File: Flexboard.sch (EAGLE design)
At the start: 324 parts, among them U1 MK20DN512VLQ10

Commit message: Routed LED ROW nets
PCB has not had led traces routed, but LED row nets are routed in
schematic
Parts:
- added SJ_LED_R1_0, SJ_LED_R2_0, SJ_LED_R2_1, SJ_LED_R3_1, SJ_LED_R4_0, SJ_LED_R4_1, SJ_LED_R5_0, SJ_LED_R5_1, SJ_LED_R6_0, SJ_LED_R6_1, SJ__LED_R3_0: (no value), jumper:SJW
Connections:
- new net LED_ROW_0: KEY_1.LED+, KEY_10.LED+, KEY_11.LED+, KEY_12.LED+, KEY_13.LED+, KEY_14.LED+, KEY_15.LED+, KEY_16.LED+, KEY_17.LED+, KEY_18.LED+, KEY_19.LED+, KEY_2.LED+, KEY_20.LED+, KEY_3.LED+, KEY_4.LED+, KEY_5.LED+, KEY_6.LED+, KEY_7.LED+, KEY_8.LED+, KEY_9.LED+
- new net LED_ROW_1: KEY_21.LED+, KEY_22.LED+, SJ_LED_R1_0.2
- new net LED_ROW_2: KEY_41.LED+, KEY_42.LED+, SJ_LED_R2_0.2
- new net LED_ROW_3: KEY_64.LED+, KEY_65.LED+, SJ__LED_R3_0.2
- new net LED_ROW_4: KEY_87.LED+, KEY_88.LED+, SJ_LED_R4_0.2
- new net LED_ROW_5: KEY_109.LED+, KEY_110.LED+, SJ_LED_R5_0.2
- new net LED_ROW_6: KEY_129.LED+, KEY_130.LED+, SJ_LED_R6_0.2
- new net N$1: KEY_66.LED+, KEY_67.LED+, KEY_68.LED+, KEY_69.LED+, KEY_70.LED+, KEY_71.LED+, KEY_72.LED+, KEY_73.LED+, KEY_74.LED+, KEY_75.LED+, KEY_76.LED+, KEY_77.LED+, KEY_78.LED+, KEY_79.LED+, KEY_80.LED+, KEY_81.LED+, KEY_82.LED+, SJ_LED_R3_1.2, SJ__LED_R3_0.1
- new net N$170: KEY_60.LED+, KEY_61.LED+, KEY_62.LED+, KEY_63.LED+, SJ_LED_R2_1.1
- new net N$173: KEY_83.LED+, KEY_84.LED+, KEY_85.LED+, KEY_86.LED+, SJ_LED_R3_1.1
- new net N$177: KEY_100.LED+, KEY_101.LED+, KEY_102.LED+, KEY_103.LED+, KEY_104.LED+, KEY_89.LED+, KEY_90.LED+, KEY_91.LED+, KEY_92.LED+, KEY_93.LED+, KEY_94.LED+, KEY_95.LED+, KEY_96.LED+, KEY_97.LED+, KEY_98.LED+, KEY_99.LED+, SJ_LED_R4_0.1, SJ_LED_R4_1.2
- new net N$179: KEY_105.LED+, KEY_106.LED+, KEY_107.LED+, KEY_108.LED+, SJ_LED_R4_1.1
- new net N$181: KEY_111.LED+, KEY_112.LED+, KEY_113.LED+, KEY_114.LED+, KEY_115.LED+, KEY_116.LED+, KEY_117.LED+, KEY_118.LED+, KEY_119.LED+, KEY_120.LED+, KEY_121.LED+, KEY_122.LED+, KEY_123.LED+, KEY_124.LED+, KEY_125.LED+, SJ_LED_R5_0.1, SJ_LED_R5_1.2
- new net N$182: KEY_126.LED+, KEY_127.LED+, KEY_128.LED+, SJ_LED_R5_1.1
- new net N$184: KEY_131.LED+, KEY_132.LED+, KEY_133.LED+, KEY_134.LED+, KEY_135.LED+, KEY_136.LED+, KEY_137.LED+, KEY_138.LED+, KEY_139.LED+, KEY_140.LED+, KEY_141.LED+, SJ_LED_R6_0.1, SJ_LED_R6_1.2
- new net N$185: KEY_142.LED+, KEY_143.LED+, KEY_144.LED+, KEY_145.LED+, SJ_LED_R6_1.1
- new net N$2: KEY_23.LED+, KEY_24.LED+, KEY_25.LED+, KEY_26.LED+, KEY_27.LED+, KEY_28.LED+, KEY_29.LED+, KEY_30.LED+, KEY_31.LED+, KEY_32.LED+, KEY_33.LED+, KEY_34.LED+, KEY_35.LED+, KEY_36.LED+, KEY_37.LED+, KEY_38.LED+, KEY_39.LED+, KEY_40.LED+, SJ_LED_R1_0.1
- new net N$61: KEY_43.LED+, KEY_44.LED+, KEY_45.LED+, KEY_46.LED+, KEY_47.LED+, KEY_48.LED+, KEY_49.LED+, KEY_50.LED+, KEY_51.LED+, KEY_52.LED+, KEY_53.LED+, KEY_54.LED+, KEY_55.LED+, KEY_56.LED+, KEY_57.LED+, KEY_58.LED+, KEY_59.LED+, SJ_LED_R2_0.1, SJ_LED_R2_1.2
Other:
- moved on the sheet: D129, D130, D131, D132, D133, D134, D135, D136, D137, D138, D139, D140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

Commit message: Routed Column Nets for LEDs
No LED traces routed on board, but all nets are routed for columns and
rows in schematic
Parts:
- added SJ_LED_C1, SJ_LED_C10, SJ_LED_C11, SJ_LED_C12, SJ_LED_C13, SJ_LED_C14, SJ_LED_C15, SJ_LED_C16, SJ_LED_C17, SJ_LED_C18, SJ_LED_C2, SJ_LED_C3, SJ_LED_C4, SJ_LED_C5, SJ_LED_C6, SJ_LED_C7, SJ_LED_C8, SJ_LED_C9: (no value), jumper:SJW
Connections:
- new net LED_COL_0: KEY_1.LED-, KEY_109.LED-, KEY_129.LED-, KEY_21.LED-, KEY_41.LED-, KEY_64.LED-, KEY_87.LED-
- new net LED_COL_1: KEY_110.LED-, KEY_130.LED-, KEY_2.LED-, KEY_22.LED-, KEY_42.LED-, KEY_65.LED-, KEY_88.LED-
- new net LED_COL_10: KEY_119.LED-, KEY_31.LED-, KEY_31_OFFSET.LED-, KEY_51.LED-, KEY_74.LED-, KEY_97.LED-, SJ_LED_C10.1
- new net LED_COL_11: KEY_120.LED-, KEY_135.LED-, KEY_32.LED-, KEY_32_OFFSET.LED-, KEY_52.LED-, KEY_75.LED-, KEY_98.LED-, SJ_LED_C11.1
- new net LED_COL_12: KEY_121.LED-, KEY_136.LED-, KEY_33.LED-, KEY_33_OFFSET.LED-, KEY_53.LED-, KEY_76.LED-, KEY_99.LED-, SJ_LED_C12.1
- new net LED_COL_13: KEY_100.LED-, KEY_137.LED-, KEY_34.LED-, KEY_54.LED-, KEY_77.LED-, SJ_LED_C13.1
- new net LED_COL_14: KEY_35.LED-, KEY_55.LED-, KEY_78.LED-, SJ_LED_C14.1
- new net LED_COL_15: KEY_36.LED-, SJ_LED_C15.1
- new net LED_COL_16: KEY_101.LED-, KEY_122.LED-, KEY_138.LED-, KEY_37.LED-, KEY_56.LED-, KEY_79.LED-, SJ_LED_C16.1
- new net LED_COL_17: KEY_102.LED-, KEY_123.LED-, KEY_139.LED-, KEY_38.LED-, KEY_57.LED-, KEY_80.LED-, SJ_LED_C17.1
- new net LED_COL_18: KEY_103.LED-, KEY_124.LED-, KEY_140.LED-, KEY_39.LED-, KEY_58.LED-, KEY_81.LED-, SJ_LED_C18.1
- new net LED_COL_19: KEY_104.LED-, KEY_125.LED-, KEY_141.LED-, KEY_40.LED-, KEY_59.LED-, KEY_82.LED-, SJ_LED_C1.1
- new net LED_COL_2: KEY_111.LED-, KEY_131.LED-, KEY_23.LED-, KEY_43.LED-, KEY_66.LED-, KEY_89.LED-, SJ_LED_C2.1
- new net LED_COL_20: KEY_105.LED-, KEY_126.LED-, KEY_142.LED-, KEY_60.LED-, KEY_83.LED-
- new net LED_COL_21: KEY_106.LED-, KEY_127.LED-, KEY_143.LED-, KEY_61.LED-, KEY_84.LED-
- new net LED_COL_22: KEY_107.LED-, KEY_128.LED-, KEY_144.LED-, KEY_62.LED-, KEY_85.LED-
- new net LED_COL_23: KEY_108.LED-, KEY_145.LED-, KEY_63.LED-, KEY_86.LED-
- new net LED_COL_3: KEY_112.LED-, KEY_132.LED-, KEY_24.LED-, KEY_44.LED-, KEY_67.LED-, KEY_90.LED-, SJ_LED_C3.1
- new net LED_COL_4: KEY_113.LED-, KEY_25.LED-, KEY_45.LED-, KEY_68.LED-, KEY_91.LED-, SJ_LED_C4.1
- new net LED_COL_5: KEY_114.LED-, SJ_LED_C5.1
- new net LED_COL_6: KEY_115.LED-, KEY_27.LED-, KEY_47.LED-, KEY_70.LED-, KEY_93.LED-, SJ_LED_C6.1
- new net LED_COL_7: KEY_116.LED-, KEY_134.LED-, KEY_28.LED-, KEY_48.LED-, KEY_71.LED-, KEY_94.LED-, SJ_LED_C7.1
- new net LED_COL_8: KEY_117.LED-, KEY_29.LED-, KEY_49.LED-, KEY_72.LED-, KEY_95.LED-, SJ_LED_C8.1
- new net LED_COL_9: KEY_118.LED-, KEY_30.LED-, KEY_30_OFFSET.LED-, KEY_50.LED-, KEY_73.LED-, KEY_96.LED-, SJ_LED_C9.1
- new net N$175: KEY_3.LED-, SJ_LED_C2.2
- new net N$186: KEY_4.LED-, SJ_LED_C3.2
- new net N$187: KEY_5.LED-, SJ_LED_C4.2
- new net N$188: KEY_6.LED-, SJ_LED_C5.2
- new net N$189: KEY_7.LED-, SJ_LED_C6.2
- new net N$190: KEY_8.LED-, SJ_LED_C7.2
- new net N$191: KEY_9.LED-, SJ_LED_C8.2
- new net N$192: KEY_10.LED-, SJ_LED_C9.2
- new net N$193: KEY_11.LED-, SJ_LED_C10.2
- new net N$194: KEY_12.LED-, SJ_LED_C11.2
- new net N$195: KEY_13.LED-, SJ_LED_C12.2
- new net N$196: KEY_14.LED-, SJ_LED_C13.2
- new net N$197: KEY_15.LED-, SJ_LED_C14.2
- new net N$198: KEY_16.LED-, SJ_LED_C15.2
- new net N$199: KEY_17.LED-, SJ_LED_C16.2
- new net N$200: KEY_18.LED-, SJ_LED_C17.2
- new net N$201: KEY_19.LED-, SJ_LED_C18.2
- new net N$202: KEY_20.LED-, SJ_LED_C1.2
- net N$1: now also KEY_69.LED-
- net N$177: now also KEY_92.LED-
- net N$2: now also KEY_26.LED-, KEY_30_OFFSET.LED+, KEY_31_OFFSET.LED+, KEY_32_OFFSET.LED+, KEY_33_OFFSET.LED+
- net N$61: now also KEY_46.LED-
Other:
- moved on the sheet: D1, D10, D100, D101, D102, D103, D104, D105, D106, D107, D108, D109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

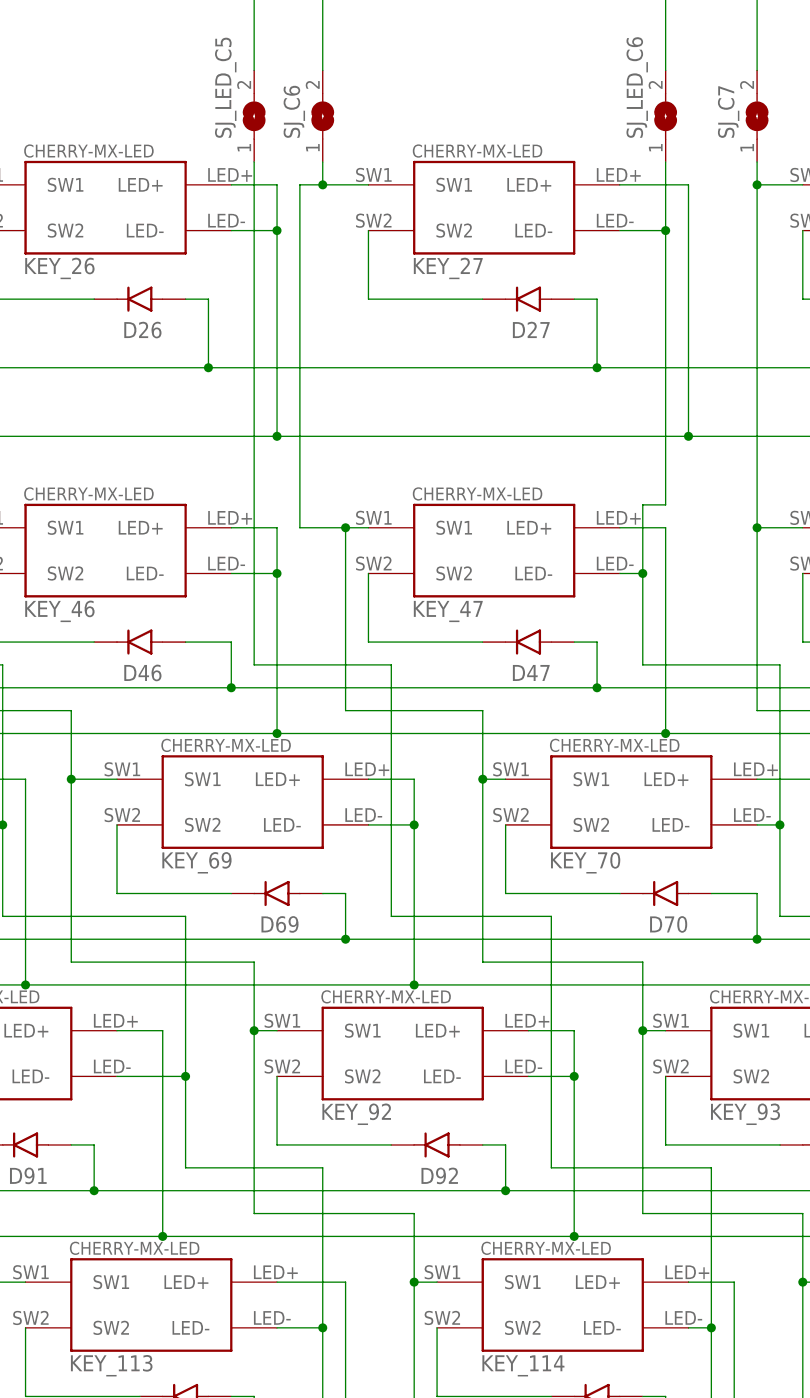
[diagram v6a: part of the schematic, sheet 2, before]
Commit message: Routed LED columns, rows partially routed
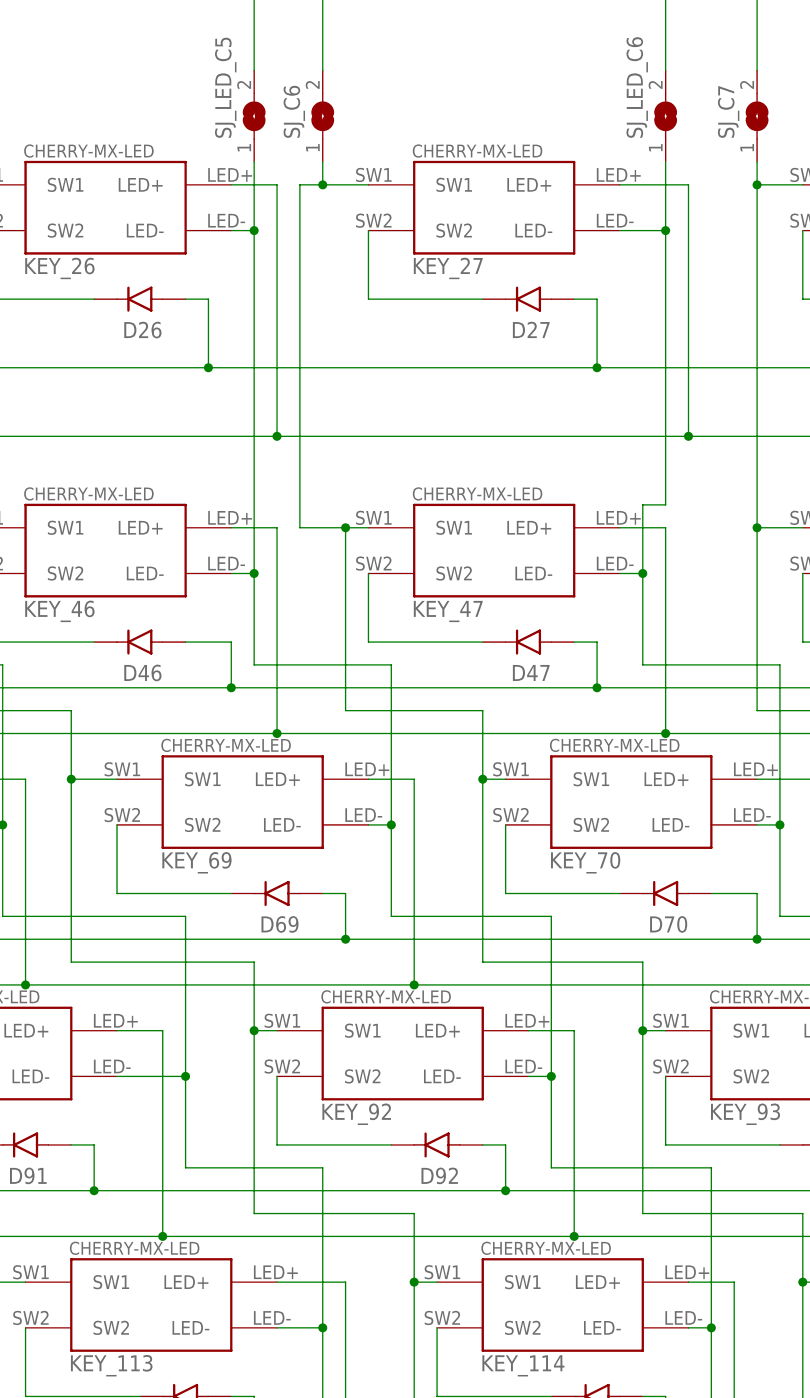
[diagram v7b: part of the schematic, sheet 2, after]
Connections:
- net LED_COL_5: now also KEY_26.LED-, KEY_46.LED-, KEY_69.LED-, KEY_92.LED-
- net N$1: no longer KEY_69.LED-
- net N$177: no longer KEY_92.LED-
- net N$2: no longer KEY_26.LED-
- net N$61: no longer KEY_46.LED-
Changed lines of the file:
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@@
 <pinref part="KEY_26" gate="G$1" pin="LED+"/>
 <wire x1="269.24" y1="-30.48" x2="274.32" y2="-30.48" width="0.1524" layer="91"/>
-<wire x1="274.32" y1="-30.48" x2="274.32" y2="-35.56" width="0.1524" layer="91"/>
 <junction x="274.32" y="-58.42"/>
 <pinref part="KEY_25" gate="G$1" pin="LED+"/>
-<wire x1="274.32" y1="-35.56" x2="274.32" y2="-58.42" width="0.1524" layer="91"/>
+<wire x1="274.32" y1="-30.48" x2="274.32" y2="-58.42" width="0.1524" layer="91"/>
 <wire x1="223.52" y1="-30.48" x2="228.6" y2="-30.48" width="0.1524" layer="91"/>
 <wire x1="228.6" y1="-30.48" x2="228.6" y2="-58.42" width="0.1524" layer="91"/>
@@
 <wire x1="579.12" y1="-12.7" x2="579.12" y2="-30.48" width="0.1524" layer="91"/>
 <junction x="579.12" y="-30.48"/>
-<pinref part="KEY_26" gate="G$1" pin="LED-"/>
-<wire x1="269.24" y1="-35.56" x2="274.32" y2="-35.56" width="0.1524" layer="91"/>
-<junction x="274.32" y="-35.56"/>
 </segment>
 </net>
@@
 <pinref part="KEY_46" gate="G$1" pin="LED+"/>
 <wire x1="269.24" y1="-68.58" x2="274.32" y2="-68.58" width="0.1524" layer="91"/>
-<wire x1="274.32" y1="-68.58" x2="274.32" y2="-73.66" width="0.1524" layer="91"/>
 <junction x="274.32" y="-91.44"/>
 <pinref part="KEY_47" gate="G$1" pin="LED+"/>
-<wire x1="274.32" y1="-73.66" x2="274.32" y2="-91.44" width="0.1524" layer="91"/>
+<wire x1="274.32" y1="-68.58" x2="274.32" y2="-91.44" width="0.1524" layer="91"/>
 <wire x1="312.42" y1="-68.58" x2="317.5" y2="-68.58" width="0.1524" layer="91"/>
 <wire x1="317.5" y1="-68.58" x2="317.5" y2="-91.44" width="0.1524" layer="91"/>
@@
 <wire x1="896.62" y1="-78.74" x2="896.62" y2="-91.44" width="0.1524" layer="91"/>
 <junction x="896.62" y="-91.44"/>
-<pinref part="KEY_46" gate="G$1" pin="LED-"/>
-<wire x1="269.24" y1="-73.66" x2="274.32" y2="-73.66" width="0.1524" layer="91"/>
-<junction x="274.32" y="-73.66"/>
 </segment>
 </net>
@@
 <pinref part="KEY_69" gate="G$1" pin="LED+"/>
 <wire x1="284.48" y1="-96.52" x2="289.56" y2="-96.52" width="0.1524" layer="91"/>
-<wire x1="289.56" y1="-96.52" x2="289.56" y2="-101.6" width="0.1524" layer="91"/>
 <junction x="289.56" y="-119.38"/>
 <pinref part="KEY_68" gate="G$1" pin="LED+"/>
-<wire x1="289.56" y1="-101.6" x2="289.56" y2="-119.38" width="0.1524" layer="91"/>
+<wire x1="289.56" y1="-96.52" x2="289.56" y2="-119.38" width="0.1524" layer="91"/>
 <wire x1="238.76" y1="-96.52" x2="246.38" y2="-96.52" width="0.1524" layer="91"/>
 <wire x1="246.38" y1="-96.52" x2="246.38" y2="-119.38" width="0.1524" layer="91"/>
@@
 <wire x1="134.62" y1="-96.52" x2="134.62" y2="-119.38" width="0.1524" layer="91"/>
 <junction x="134.62" y="-119.38"/>
-<pinref part="KEY_69" gate="G$1" pin="LED-"/>
-<wire x1="284.48" y1="-101.6" x2="289.56" y2="-101.6" width="0.1524" layer="91"/>
-<junction x="289.56" y="-101.6"/>
 </segment>
 </net>
@@
 <pinref part="KEY_92" gate="G$1" pin="LED+"/>
 <wire x1="302.26" y1="-124.46" x2="307.34" y2="-124.46" width="0.1524" layer="91"/>
-<wire x1="307.34" y1="-124.46" x2="307.34" y2="-129.54" width="0.1524" layer="91"/>
 <junction x="307.34" y="-147.32"/>
 <pinref part="KEY_91" gate="G$1" pin="LED+"/>
-<wire x1="307.34" y1="-129.54" x2="307.34" y2="-147.32" width="0.1524" layer="91"/>
+<wire x1="307.34" y1="-124.46" x2="307.34" y2="-147.32" width="0.1524" layer="91"/>
 <wire x1="256.54" y1="-124.46" x2="261.62" y2="-124.46" width="0.1524" layer="91"/>
 <wire x1="261.62" y1="-124.46" x2="261.62" y2="-147.32" width="0.1524" layer="91"/>
@@
 <wire x1="134.62" y1="-124.46" x2="134.62" y2="-147.32" width="0.1524" layer="91"/>
 <junction x="134.62" y="-147.32"/>
-<pinref part="KEY_92" gate="G$1" pin="LED-"/>
-<wire x1="307.34" y1="-129.54" x2="302.26" y2="-129.54" width="0.1524" layer="91"/>
-<junction x="307.34" y="-129.54"/>
 </segment>
 </net>
@@
 <segment>
 <pinref part="SJ_LED_C5" gate="1" pin="1"/>
-<wire x1="271.78" y1="-27.94" x2="271.78" y2="-83.82" width="0.1524" layer="91"/>
+<wire x1="271.78" y1="-27.94" x2="271.78" y2="-35.56" width="0.1524" layer="91"/>
+<wire x1="271.78" y1="-35.56" x2="271.78" y2="-73.66" width="0.1524" layer="91"/>
+<wire x1="271.78" y1="-73.66" x2="271.78" y2="-83.82" width="0.1524" layer="91"/>
 <wire x1="271.78" y1="-83.82" x2="287.02" y2="-83.82" width="0.1524" layer="91"/>
-<wire x1="287.02" y1="-83.82" x2="287.02" y2="-111.76" width="0.1524" layer="91"/>
+<wire x1="287.02" y1="-83.82" x2="287.02" y2="-101.6" width="0.1524" layer="91"/>
+<wire x1="287.02" y1="-101.6" x2="287.02" y2="-111.76" width="0.1524" layer="91"/>
 <wire x1="287.02" y1="-111.76" x2="304.8" y2="-111.76" width="0.1524" layer="91"/>
-<wire x1="304.8" y1="-111.76" x2="304.8" y2="-139.7" width="0.1524" layer="91"/>
+<wire x1="304.8" y1="-111.76" x2="304.8" y2="-129.54" width="0.1524" layer="91"/>
+<wire x1="304.8" y1="-129.54" x2="304.8" y2="-139.7" width="0.1524" layer="91"/>
 <wire x1="304.8" y1="-139.7" x2="322.58" y2="-139.7" width="0.1524" layer="91"/>
 <wire x1="322.58" y1="-139.7" x2="322.58" y2="-157.48" width="0.1524" layer="91"/>
@@
 <wire x1="322.58" y1="-157.48" x2="320.04" y2="-157.48" width="0.1524" layer="91"/>
 <junction x="322.58" y="-157.48"/>
-</segment>
-</net>
+<pinref part="KEY_92" gate="G$1" pin="LED-"/>
+<wire x1="302.26" y1="-129.54" x2="304.8" y2="-129.54" width="0.1524" layer="91"/>
+<junction x="304.8" y="-129.54"/>
+<pinref part="KEY_69" gate="G$1" pin="LED-"/>
+<wire x1="284.48" y1="-101.6" x2="287.02" y2="-101.6" width="0.1524" layer="91"/>
+<junction x="287.02" y="-101.6"/>
+<pinref part="KEY_46" gate="G$1" pin="LED-"/>
+<wire x1="269.24" y1="-73.66" x2="271.78" y2="-73.66" width="0.1524" layer="91"/>
+<junction x="271.78" y="-73.66"/>
+<pinref part="KEY_26" gate="G$1" pin="LED-"/>
+<wire x1="269.24" y1="-35.56" x2="271.78" y2="-35.56" width="0.1524" layer="91"/>
+<junction x="271.78" y="-35.56"/>
+</segment>
+</net>
